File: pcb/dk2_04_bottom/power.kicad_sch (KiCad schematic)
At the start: 11 parts, among them J3 Eurorack_Power, U2 AP7333-33SAG, U8 XL1509-5.0

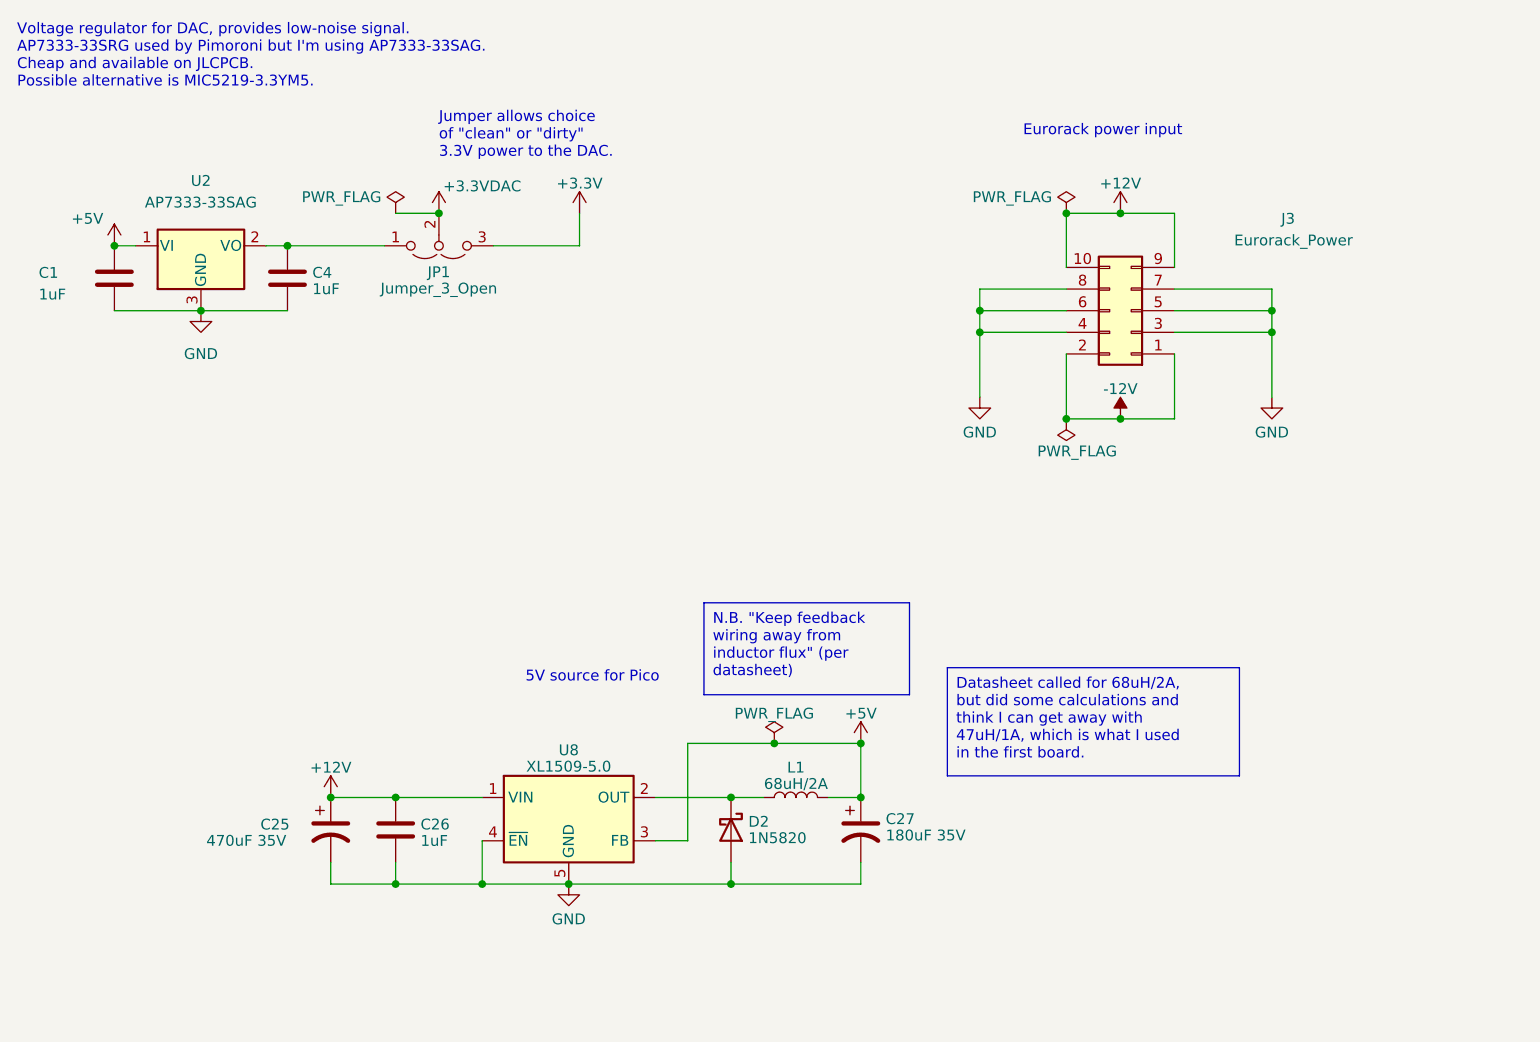
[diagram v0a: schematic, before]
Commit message: pcb 2.04 tweaks
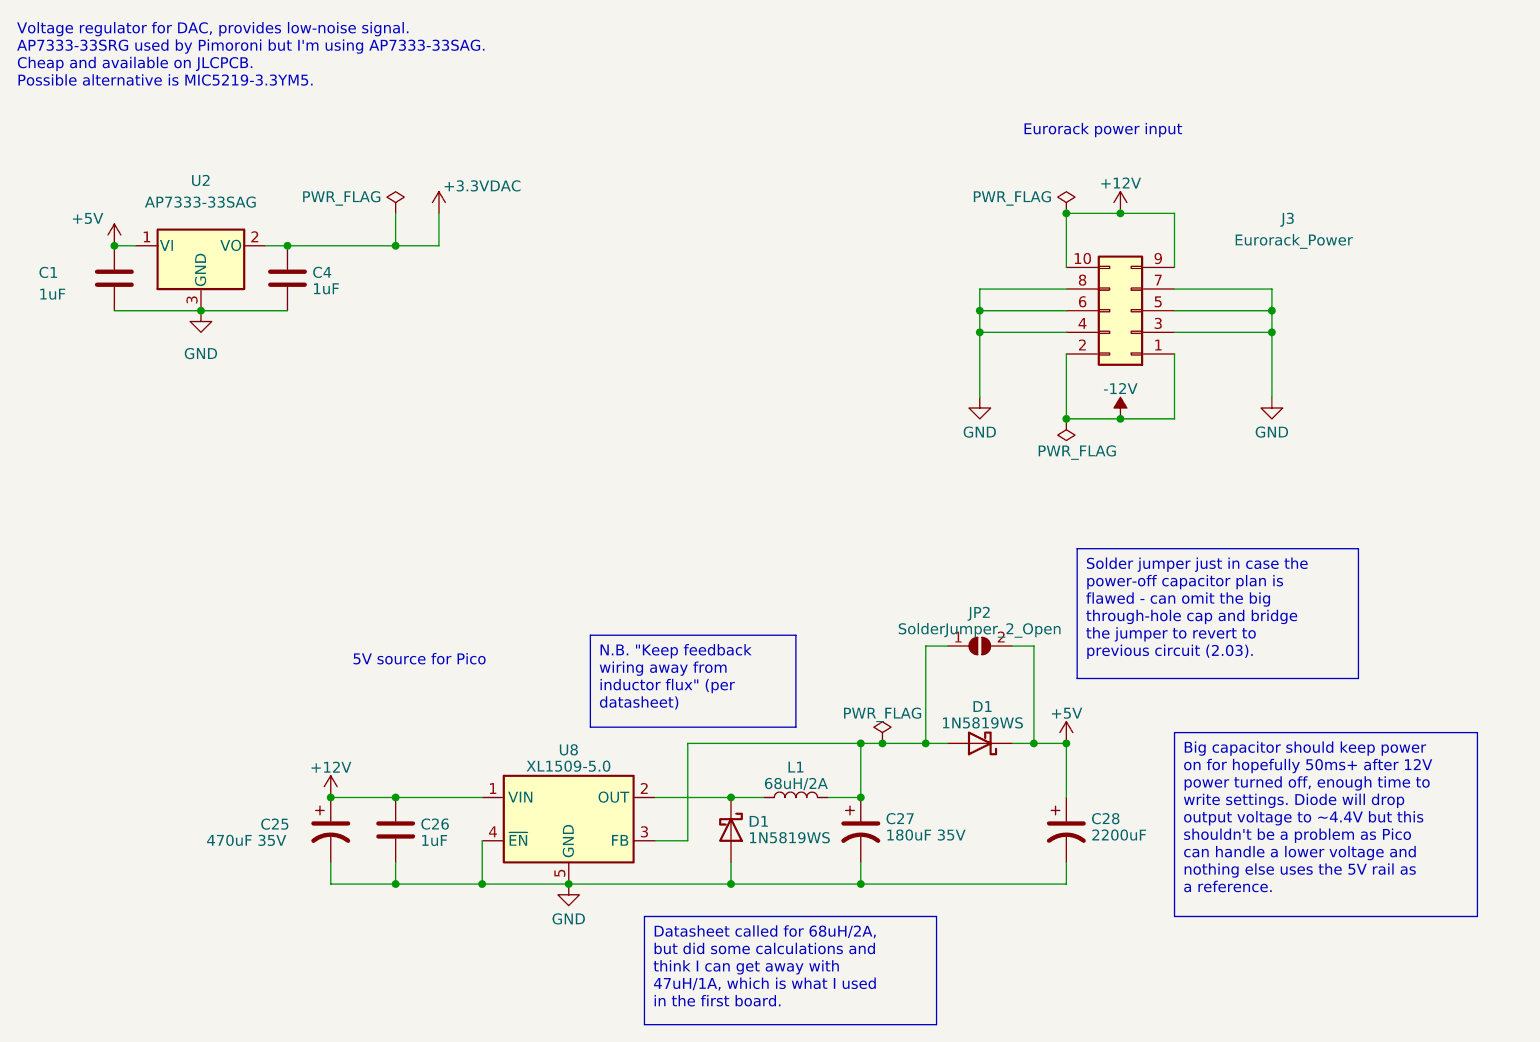
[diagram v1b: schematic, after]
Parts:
- removed D2: 1N5820, Diode_THT:D_DO-201AD_P15.24mm_Horizontal, symbol Diode:1N5820
- removed JP1: Jumper_3_Open, Connector_PinHeader_2.54mm:PinHeader_1x03_P2.54mm_Vertical, symbol Jumper:Jumper_3_Open
- added C28: 2200uF, Capacitor_THT:CP_Radial_D8.0mm_P3.50mm, symbol Device:C_Polarized_US
- added D1 (x2): 1N5819WS, Diode_SMD:D_SOD-323, symbol Diode:1N5819WS
- added JP2: SolderJumper_2_Open, Jumper:SolderJumper-2_P1.3mm_Open_Pad1.0x1.5mm, symbol Jumper:SolderJumper_2_Open
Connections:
- net +3.3VDAC: now also C4.1, U2.2 (VO)
- net +5V: now also C28.1, D1.1 (K), JP2.2 (B); no longer C27.1, L1.2, U8.3 (FB)
- net GND: now also C28.2, D1.2 (A)
- net at L1.1, U8.2 (OUT): now also D1.1 (K)
- new net: C27.1, D1.2 (A), JP2.1 (A), L1.2, U8.3 (FB)
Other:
- note removed: "Jumper allows choice of "clean" or "dirty" 3.3V power to the DAC."

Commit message: autosave works
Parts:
- C28: footprint Capacitor_THT:CP_Radial_D8.0mm_P3.50mm -> Capacitor_THT:CP_Radial_D13.0mm_P5.00mm
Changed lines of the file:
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@@
   (junction (at 215.9 66.04) (diameter 0) (color 0 0 0 0)
   )
-  (junction (at 113.03 55.88) (diameter 0) (color 0 0 0 0)
-  )
   (junction (at 198.12 52.07) (diameter 0) (color 0 0 0 0)
   )
@@
     (stroke (width 0) (type default))
   )
-  (wire (pts (xy 113.03 55.88) (xy 118.11 55.88))
-    (stroke (width 0) (type default))
-  )
   (wire (pts (xy 181.61 60.96) (xy 181.61 63.5))
     (stroke (width 0) (type default))
@@
     (stroke (width 0) (type default))
   )
-  (wire (pts (xy 113.03 52.07) (xy 113.03 55.88))
-    (stroke (width 0) (type default))
-  )
   (wire (pts (xy 177.8 102.87) (xy 175.26 102.87))
     (stroke (width 0) (type default))
@@
     (stroke (width 0) (type default))
   )
-  (wire (pts (xy 100.33 55.88) (xy 113.03 55.88))
+  (wire (pts (xy 100.33 55.88) (xy 118.11 55.88))
     (stroke (width 0) (type default))
   )
@@
       (effects (font (size 1.27 1.27)) (justify left))
     )
-    (property "Footprint" "Capacitor_THT:CP_Radial_D8.0mm_P3.50mm" (at 191.77 124.46 0)
+    (property "Footprint" "Capacitor_THT:CP_Radial_D13.0mm_P5.00mm" (at 191.77 124.46 0)
       (effects (font (size 1.27 1.27)) hide)
     )
@@
         )
       )
-    )
-  )
-  (symbol (lib_id "power:PWR_FLAG") (at 113.03 52.07 0) (unit 1)
-    (in_bom yes) (on_board yes) (dnp no)
-    (property "Reference" "#FLG07" (at 113.03 50.165 0)
-      (effects (font (size 1.27 1.27)) hide)
-    )
-    (property "Value" "PWR_FLAG" (at 106.68 50.165 0)
-      (effects (font (size 1.27 1.27)))
-    )
-    (property "Footprint" "" (at 113.03 52.07 0)
-      (effects (font (size 1.27 1.27)) hide)
-    )
-    (property "Datasheet" "~" (at 113.03 52.07 0)
-      (effects (font (size 1.27 1.27)) hide)
-    )
-    (pin "1")
-    (instances
-      (project "dk2_04_bottom"
-        (path "/87a59a99-d509-467e-85da-26d34072acb7/be1ddc4d-f499-4b75-b4b5-b626a320d90d"
-          (reference "#FLG07") (unit 1)
-        )
-      )
